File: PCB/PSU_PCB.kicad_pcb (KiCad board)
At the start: 2 copper layers, 50 x 100 mm, 118 parts, among them P1 Bluetooth HM-10, P2 ISP, P3 V+, P4 V-, Q1 IRLML0030TRPBF, Q2 IRLML0030TRPBF, SW1 SW_PUSH_SMALL_H, U1 OPA2170, U10 LT3080, U11 LM334M, U2 USB_TYPE_C, U3 ATMEGA32U4RC-A, U4 MCP41010, U5 LT1370, U6 MAX6610, U7 OPA4170, U8 INA219, U9 MCP1252, Y1 16Mhz

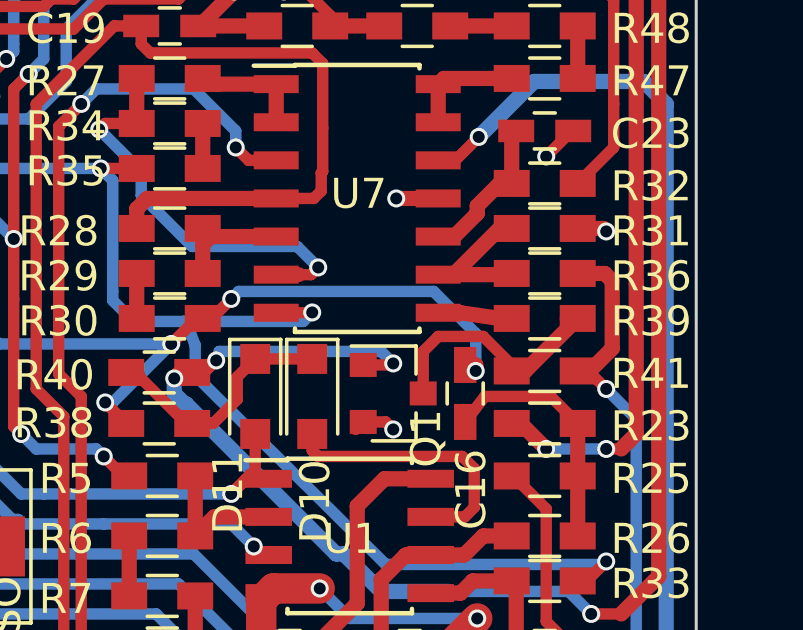
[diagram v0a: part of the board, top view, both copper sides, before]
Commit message: Fixed minor PCB error Adjusted code for current measurement
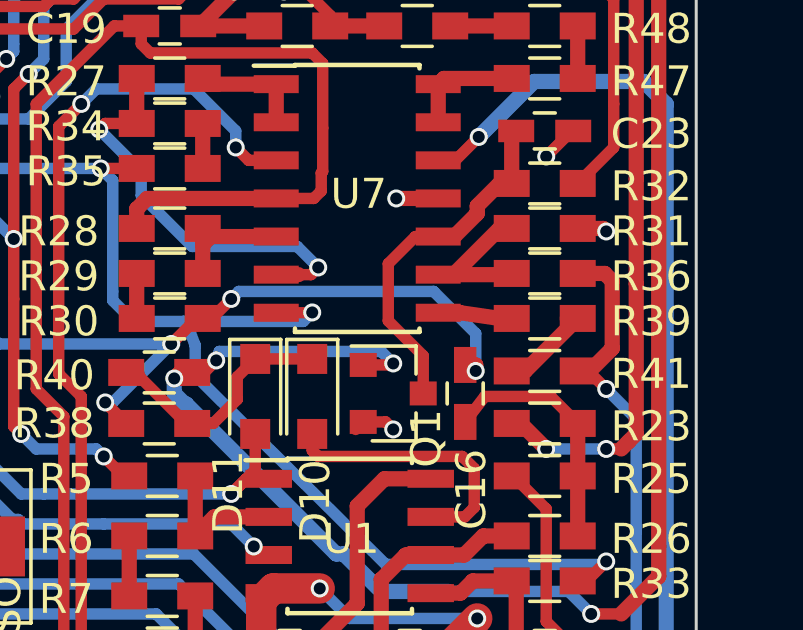
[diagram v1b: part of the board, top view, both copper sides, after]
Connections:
- P1 pad 1: (no net) -> Net-(P1-Pad1)
- P1 pad 6: (no net) -> Net-(P1-Pad6)
- Q1 pad 3: Net-(Q1-Pad3) -> Net-(C23-Pad2)
- R39 pad 1: Net-(Q1-Pad3) -> Net-(R39-Pad1)
- R41 pad 1: Net-(Q1-Pad3) -> Net-(R39-Pad1)
- U10 pad 1: (no net) -> Net-(U10-Pad1)
- U11 pad 2: (no net) -> Net-(U11-Pad2)
- U11 pad 5: (no net) -> Net-(U11-Pad5)
- U11 pad 6: (no net) -> Net-(U11-Pad6)
- U11 pad 7: (no net) -> Net-(U11-Pad7)
- U11 pad 8: (no net) -> Net-(U11-Pad8)
- U2 pad A10: (no net) -> Net-(U2-PadA10)
- U2 pad A11: (no net) -> Net-(U2-PadA11)
- U2 pad A2: (no net) -> Net-(U2-PadA2)
- U2 pad A3: (no net) -> Net-(U2-PadA3)
- U2 pad A8: (no net) -> Net-(U2-PadA8)
- U2 pad B10: (no net) -> Net-(U2-PadB10)
- U2 pad B11: (no net) -> Net-(U2-PadB11)
- U2 pad B2: (no net) -> Net-(U2-PadB2)
- U2 pad B3: (no net) -> Net-(U2-PadB3)
- U2 pad B8: (no net) -> Net-(U2-PadB8)
- U4 pad 7: (no net) -> Net-(U4-Pad7)
- U5 pad 6: (no net) -> Net-(U5-Pad6)
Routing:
- net Net-(Q1-Pad3): track 8.43 -> 0.00 mm
- net Net-(C23-Pad2): track 5.14 -> 12.0 mm
- net Net-(R39-Pad1): track 0.00 -> 3.47 mm
